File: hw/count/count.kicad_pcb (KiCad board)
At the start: 2 copper layers, 38.4 x 58.9 mm, 22 parts, among them J1 conn_trigger, J2 conn_done, J3 FTDI, J4 Conn_01x01_Male, J5 Conn_01x01_Male, J6 Conn_01x01_Male, J7 Conn_01x01_Male, SW1 reset_count, SW3 switch_reset, U1 ATmega328P-PU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

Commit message: update hardware
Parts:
- removed J4, J5, J6: Conn_01x01_Male, Connector_PinHeader_2.54mm:PinHeader_1x01_P2.54mm_Vertical
- moved C3 11.4 mm to (159.0, 75.9), turned to 180 degrees
- moved SW1 5.17 mm to (135.8, 115.5)
- moved Y1 4.28 mm to (151.4, 80.3)
- moved C2 3.22 mm to (149.1, 75.9), turned to 0 degrees
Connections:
- H1 pad 1: GND -> Net-(H1-Pad1)
- H2 pad 1: GND -> Net-(H2-Pad1)
- H3 pad 1: GND -> Net-(H3-Pad1)
- H4 pad 1: GND -> Net-(H4-Pad1)
- SW1 pad 4: Net-(SW1-Pad3) -> Net-(SW1-Pad4)
- SW3 pad 4: Net-(SW3-Pad3) -> Net-(SW3-Pad4)
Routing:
- net GND: track 186.2 -> 155.7 mm
- net XTAL2: track 30.1 -> 20.3 mm
- net a3: track 26.7 -> 32.2 mm
- net d11: track 5.12 -> 0.00 mm
- net d10: track 4.60 -> 0.00 mm
- net Net-(SW3-Pad3): track 4.50 -> 0.00 mm
- net Net-(SW1-Pad3): track 4.50 -> 0.00 mm
- net d9: track 4.16 -> 0.00 mm
- net VCC: track 127.8 -> 130.1 mm
- net d13: track 37.9 -> 38.5 mm
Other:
- board text added: "v1.1"
- board text removed: "v1"

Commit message: COUNT block v2
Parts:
- removed J2: conn_done, Connector_PinHeader_2.54mm:PinHeader_1x03_P2.54mm_Vertical
- removed J7: Conn_01x01_Male, Connector_PinHeader_2.54mm:PinHeader_1x01_P2.54mm_Vertical
- removed SW1: reset_count, autoblocks:SW_PUSH_6mm_H5mm
- added D2: DIODE, Diode_SMD:D_0603_1608Metric, F.Cu at (133.5, 122.4)
- added J5: BUS, Connector_PinHeader_2.54mm:PinHeader_2x07_P2.54mm_Vertical, F.Cu at (149.1, 95.0)
- added R4: 10k, Resistor_SMD:R_0603_1608Metric, F.Cu at (146.2, 113.4)
- added R5: 1k, Resistor_SMD:R_0603_1608Metric, F.Cu at (137.4, 122.5)
- added R6: 1k, Resistor_SMD:R_0603_1608Metric, F.Cu at (141.3, 122.4)
- added R7: 1k, Resistor_SMD:R_0603_1608Metric, F.Cu at (146.5, 123.5)
- added SW2: resetCount, autoblocks:SW_PUSH_6mm_H5mm, B.Cu at (138.2, 164.6)
- added SW4: NEXT, Package_DIP:DIP-16_W7.62mm_SMDSocket_SmallPads, F.Cu at (136.4, 141.7)
- added SW6: ID, Package_DIP:DIP-16_W7.62mm_SMDSocket_SmallPads, F.Cu at (136.4, 153.2)
- C1: footprint Capacitor_THT:CP_Radial_Tantal_D6.0mm_P2.50mm -> Capacitor_SMD:C_0603_1608Metric
- C2, C3: footprint Capacitor_THT:C_Disc_D3.0mm_W1.6mm_P2.50mm -> Capacitor_SMD:C_0603_1608Metric
- C4, C5: footprint Capacitor_THT:C_Axial_L5.1mm_D3.1mm_P7.50mm_Horizontal -> Capacitor_SMD:C_0603_1608Metric
- H1, H2, H3, H4: footprint MountingHole:MountingHole_2.2mm_M2 -> MountingHole:MountingHole_3.2mm_M3_Pad
- J1: value conn_trigger -> bootloader; footprint Connector_PinHeader_2.54mm:PinHeader_1x03_P2.54mm_Vertical -> autoblocks:edge_connector_3
- J3: footprint Connector_PinHeader_2.54mm:PinHeader_1x06_P2.54mm_Vertical -> autoblocks:edge_connector_3
- R2: footprint Resistor_THT:R_Axial_DIN0207_L6.3mm_D2.5mm_P10.16mm_Horizontal -> Resistor_SMD:R_0603_1608Metric
- SW3: value switch_reset -> reset; footprint autoblocks:SW_PUSH_6mm_H5mm -> Button_Switch_SMD:SW_SPST_TL3305C
- U1: value ATmega328P-PU -> ATmega328-AU; footprint Package_DIP:DIP-28_W7.62mm -> Package_QFP:TQFP-32_7x7mm_P0.8mm
- U2: moved to B.Cu
- Y1: footprint Crystal:Crystal_HC18-U_Vertical -> Crystal:Crystal_SMD_HC49-SD
- moved H2 103.1 mm to (128.0, 166.6)
- moved H1 102.4 mm to (154.7, 166.6)
- moved C3 47.2 mm to (146.5, 121.4), turned to 0 degrees
- moved C2 43.6 mm to (146.3, 119.4)
- moved H4 39.7 mm to (128.0, 96.8)
- moved Y1 37.5 mm to (152.4, 117.8), turned to 270 degrees
- moved H3 37.3 mm to (154.7, 96.8)
- moved U2 31.9 mm to (143.3, 134.1)
- moved C5 30.5 mm to (136.9, 103.1), turned to 0 degrees
- moved C1 26.6 mm to (146.3, 117.5), turned to 180 degrees
- moved C4 25.8 mm to (136.9, 106.9), turned to 180 degrees
- moved R2 24.7 mm to (133.1, 106.8), turned to 180 degrees
- moved U1 24.6 mm to (137.7, 114.7)
- moved SW3 23.9 mm to (130.1, 103.4), turned to 180 degrees
- moved J3 12.9 mm to (126.5, 109.5), turned to 270 degrees
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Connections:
- C1 pad 1: VCC -> bus11
- C1 pad 2: GND -> bus13
- C2 pad 1: GND -> bus13
- C3 pad 1: GND -> bus13
- C4 pad 2: GND -> bus13
- J1 pad 1: a0 -> bus13
- J1 pad 2: GND -> bus11
- J1 pad 3: VCC -> d10
- J3 pad 1: GND -> bus13
- J3 pad 2: GND -> bus13
- J3 pad 3: VCC -> bus11
- R2 pad 1: VCC -> bus11
- SW3 pad 1: GND -> bus13
- U1 pad 1: RESET -> d3
- U1 pad 10: XTAL2 -> d6
- U1 pad 11: d5 -> d7
- U1 pad 12: d6 -> d8
- U1 pad 13: d7 -> d9
- U1 pad 14: d8 -> d10
- U1 pad 15: d9 -> d11
- U1 pad 16: d10 -> d12
- U1 pad 17: d11 -> d13
- U1 pad 18: d12 -> bus11
- U1 pad 19: d13 -> Net-(U1-Pad19)
- U1 pad 2: RX -> d4
- U1 pad 20: VCC -> AREF
- U1 pad 21: AREF -> bus13
- U1 pad 22: GND -> Net-(U1-Pad22)
- U1 pad 3: TX -> bus13
- U1 pad 4: d2 -> bus11
- U1 pad 5: d3 -> bus13
- U1 pad 6: d4 -> bus11
- U1 pad 7: VCC -> XTAL1
- U1 pad 8: GND -> XTAL2
- U1 pad 9: XTAL1 -> d5
- U2 pad 1: d13 -> Net-(R5-Pad2)
- U2 pad 5: a4 -> Net-(R6-Pad2)
- U2 pad 7: a5 -> Net-(R7-Pad2)
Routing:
- net GND: track 155.7 -> 0.00 mm
- net d10: track 0.00 -> 132.1 mm, vias 0 -> 2
- net VCC: track 130.1 -> 0.00 mm
- net bus11: track 0.00 -> 126.7 mm, vias 0 -> 7
- net d11: track 0.00 -> 101.0 mm, vias 0 -> 1
- net d12: track 22.1 -> 107.6 mm, vias 0 -> 2
- net bus2: track 0.00 -> 69.1 mm, vias 0 -> 1
- net bus3: track 0.00 -> 63.8 mm, vias 0 -> 1
- net bus13: track 0.00 -> 63.6 mm, vias 0 -> 6
- net bus5: track 0.00 -> 62.7 mm, vias 0 -> 1
- net bus4: track 0.00 -> 61.4 mm, vias 0 -> 1
- net bus7: track 0.00 -> 61.2 mm, vias 0 -> 1
- net bus1: track 0.00 -> 60.8 mm, vias 0 -> 1
- net bus6: track 0.00 -> 60.3 mm, vias 0 -> 1
- net bus8: track 0.00 -> 59.2 mm, vias 0 -> 1
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- added copper zone on B.Cu, net bus11
- added copper zone on F.Cu, net bus13
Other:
- board size 38.4 x 58.9 mm -> 34.3 x 77.5 mm
- rule trace_min: 0.2 -> 0.16
- board text added: "BOOT"
- board text added: "FTDI"
- board text added: "First"
- board text added: "ID"
- board text added: "NEXT"
- board text added: "Next"
- board text added: "RESET COUNT"
- board text added: "v2"
- board text removed: "COUNTER"
- board text removed: "IN"
- board text removed: "OUT"
- board text removed: "RESET"
- board text removed: "RTS"
- board text removed: "v1.1"

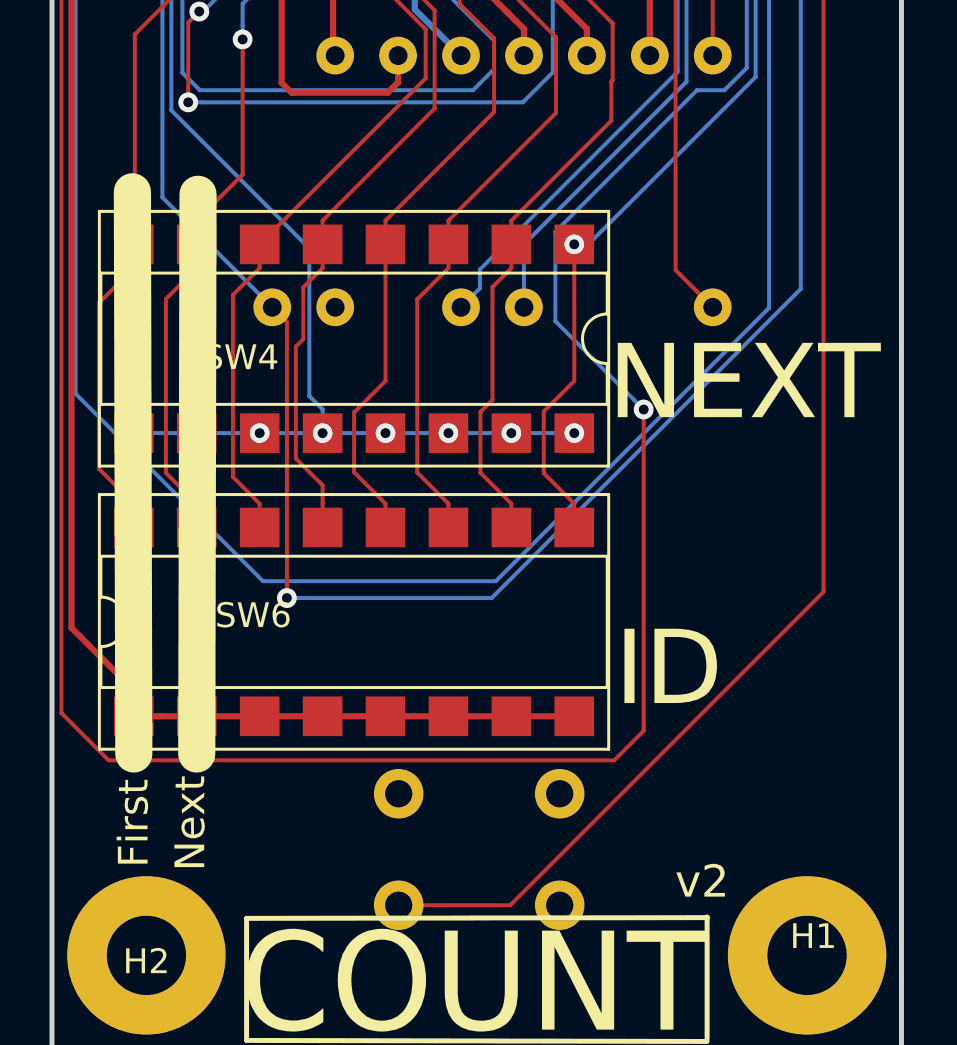
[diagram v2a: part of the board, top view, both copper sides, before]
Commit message: fix COUNT bus assigments
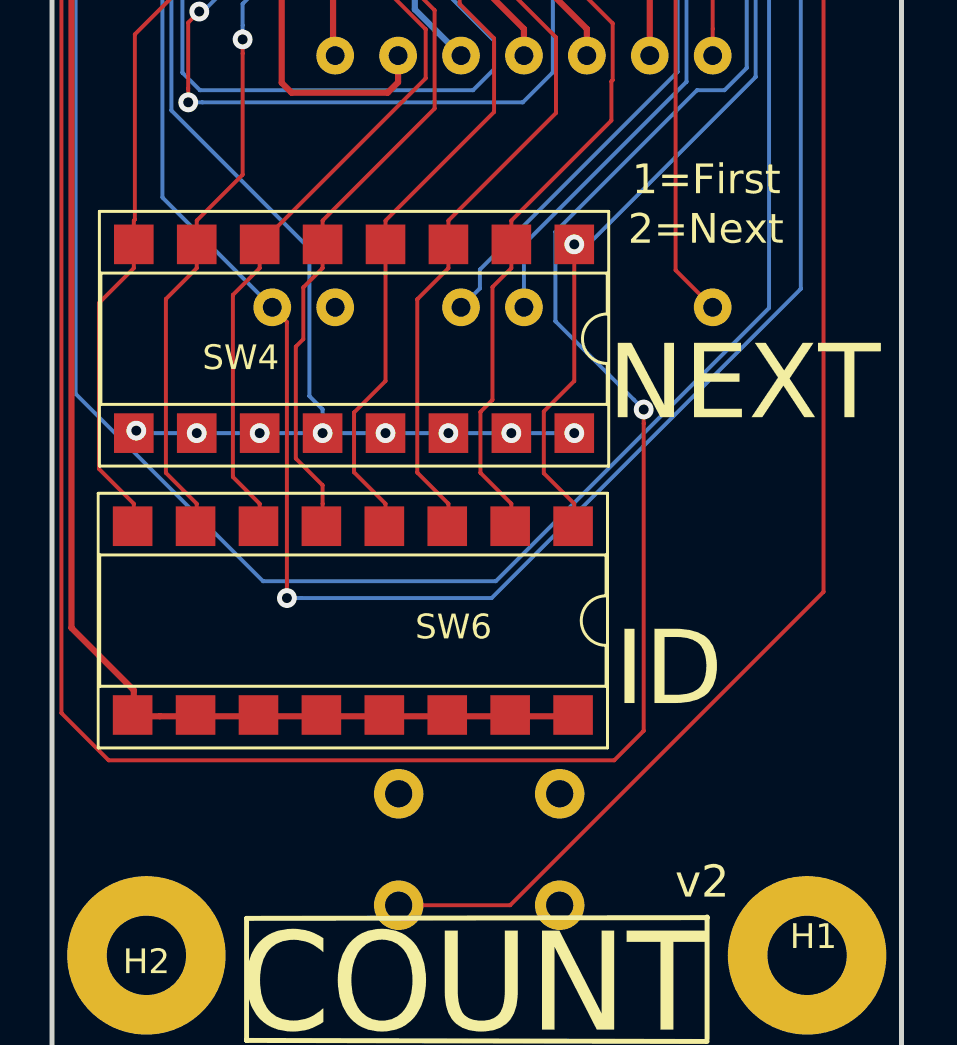
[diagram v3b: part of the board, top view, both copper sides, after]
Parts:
- moved SW6 0.07 mm to (136.3, 153.1), turned to 270 degrees
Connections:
- SW6 pad 1: a0 -> bus1
- SW6 pad 10: bus2 -> a0
- SW6 pad 11: bus3 -> a0
- SW6 pad 12: bus4 -> a0
- SW6 pad 13: bus5 -> a0
- SW6 pad 14: bus6 -> a0
- SW6 pad 15: bus7 -> a0
- SW6 pad 16: bus8 -> a0
- SW6 pad 2: a0 -> bus2
- SW6 pad 3: a0 -> bus3
- SW6 pad 4: a0 -> bus4
- SW6 pad 5: a0 -> bus5
- SW6 pad 6: a0 -> bus6
- SW6 pad 7: a0 -> bus7
- SW6 pad 8: a0 -> bus8
- SW6 pad 9: bus1 -> a0
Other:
- board text added: "1=First"
- board text added: "2=Next"
- board text removed: "First"
- board text removed: "Next"
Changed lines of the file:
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@@
   (general
     (thickness 1.6)
-    (drawings 27)
+    (drawings 25)
     (tracks 679)
     (zones 0)
@@
   )
   (setup
-    (last_trace_width 0.16)
+    (last_trace_width 0.25)
     (user_trace_width 0.16)
     (user_trace_width 1)
@@
   )
   (module Package_DIP:DIP-16_W7.62mm_SMDSocket_SmallPads (layer F.Cu)
-    (at 136.398 153.162 90)
+    (at 136.35 153.11 270)
     (descr "16-lead though-hole mounted DIP package, row spacing 7.62 mm (300 mils), SMDSocket, SmallPads")
     (tags "THT DIP DIL PDIP 2.54mm 7.62mm 300mil SMDSocket SmallPads")
     (attr smd)
-    (fp_text reference SW6 (at 0.254 -4.064 180) (layer F.SilkS)
-      (effects (font (size 1 1) (thickness 0.15)))
-    )
-    (fp_text value ID (at 0 11.22 90) (layer F.Fab)
+    (fp_text reference SW6 (at 0.254 -4.064) (layer F.SilkS)
+      (effects (font (size 1 1) (thickness 0.15)))
+    )
+    (fp_text value ID (at 0 11.22 270) (layer F.Fab)
       (effects (font (size 1 1) (thickness 0.15)))
     )
@@
     (fp_line (start 5.35 10.5) (end 5.35 -10.5) (layer F.CrtYd) (width 0.05))
     (fp_line (start 5.35 -10.5) (end -5.35 -10.5) (layer F.CrtYd) (width 0.05))
-    (fp_text user %R (at 0 0 90) (layer F.Fab)
-      (effects (font (size 1 1) (thickness 0.15)))
-    )
-    (pad 1 smd rect (at -3.81 -8.89 90) (size 1.6 1.6) (layers F.Cu F.Paste F.Mask)
+    (fp_text user %R (at 0 0 270) (layer F.Fab)
+      (effects (font (size 1 1) (thickness 0.15)))
+    )
+    (pad 1 smd rect (at -3.81 -8.89 270) (size 1.6 1.6) (layers F.Cu F.Paste F.Mask)
+      (net 33 bus1))
+    (pad 9 smd rect (at 3.81 8.89 270) (size 1.6 1.6) (layers F.Cu F.Paste F.Mask)
       (net 6 a0))
-    (pad 9 smd rect (at 3.81 8.89 90) (size 1.6 1.6) (layers F.Cu F.Paste F.Mask)
-      (net 33 bus1))
-    (pad 2 smd rect (at -3.81 -6.35 90) (size 1.6 1.6) (layers F.Cu F.Paste F.Mask)
+    (pad 2 smd rect (at -3.81 -6.35 270) (size 1.6 1.6) (layers F.Cu F.Paste F.Mask)
+      (net 34 bus2))
+    (pad 10 smd rect (at 3.81 6.35 270) (size 1.6 1.6) (layers F.Cu F.Paste F.Mask)
       (net 6 a0))
-    (pad 10 smd rect (at 3.81 6.35 90) (size 1.6 1.6) (layers F.Cu F.Paste F.Mask)
-      (net 34 bus2))
-    (pad 3 smd rect (at -3.81 -3.81 90) (size 1.6 1.6) (layers F.Cu F.Paste F.Mask)
+    (pad 3 smd rect (at -3.81 -3.81 270) (size 1.6 1.6) (layers F.Cu F.Paste F.Mask)
+      (net 35 bus3))
+    (pad 11 smd rect (at 3.81 3.81 270) (size 1.6 1.6) (layers F.Cu F.Paste F.Mask)
       (net 6 a0))
-    (pad 11 smd rect (at 3.81 3.81 90) (size 1.6 1.6) (layers F.Cu F.Paste F.Mask)
-      (net 35 bus3))
-    (pad 4 smd rect (at -3.81 -1.27 90) (size 1.6 1.6) (layers F.Cu F.Paste F.Mask)
+    (pad 4 smd rect (at -3.81 -1.27 270) (size 1.6 1.6) (layers F.Cu F.Paste F.Mask)
+      (net 36 bus4))
+    (pad 12 smd rect (at 3.81 1.27 270) (size 1.6 1.6) (layers F.Cu F.Paste F.Mask)
       (net 6 a0))
-    (pad 12 smd rect (at 3.81 1.27 90) (size 1.6 1.6) (layers F.Cu F.Paste F.Mask)
-      (net 36 bus4))
-    (pad 5 smd rect (at -3.81 1.27 90) (size 1.6 1.6) (layers F.Cu F.Paste F.Mask)
+    (pad 5 smd rect (at -3.81 1.27 270) (size 1.6 1.6) (layers F.Cu F.Paste F.Mask)
+      (net 37 bus5))
+    (pad 13 smd rect (at 3.81 -1.27 270) (size 1.6 1.6) (layers F.Cu F.Paste F.Mask)
       (net 6 a0))
-    (pad 13 smd rect (at 3.81 -1.27 90) (size 1.6 1.6) (layers F.Cu F.Paste F.Mask)
-      (net 37 bus5))
-    (pad 6 smd rect (at -3.81 3.81 90) (size 1.6 1.6) (layers F.Cu F.Paste F.Mask)
+    (pad 6 smd rect (at -3.81 3.81 270) (size 1.6 1.6) (layers F.Cu F.Paste F.Mask)
+      (net 38 bus6))
+    (pad 14 smd rect (at 3.81 -3.81 270) (size 1.6 1.6) (layers F.Cu F.Paste F.Mask)
       (net 6 a0))
-    (pad 14 smd rect (at 3.81 -3.81 90) (size 1.6 1.6) (layers F.Cu F.Paste F.Mask)
-      (net 38 bus6))
-    (pad 7 smd rect (at -3.81 6.35 90) (size 1.6 1.6) (layers F.Cu F.Paste F.Mask)
+    (pad 7 smd rect (at -3.81 6.35 270) (size 1.6 1.6) (layers F.Cu F.Paste F.Mask)
+      (net 39 bus7))
+    (pad 15 smd rect (at 3.81 -6.35 270) (size 1.6 1.6) (layers F.Cu F.Paste F.Mask)
       (net 6 a0))
-    (pad 15 smd rect (at 3.81 -6.35 90) (size 1.6 1.6) (layers F.Cu F.Paste F.Mask)
-      (net 39 bus7))
-    (pad 8 smd rect (at -3.81 8.89 90) (size 1.6 1.6) (layers F.Cu F.Paste F.Mask)
+    (pad 8 smd rect (at -3.81 8.89 270) (size 1.6 1.6) (layers F.Cu F.Paste F.Mask)
+      (net 40 bus8))
+    (pad 16 smd rect (at 3.81 -8.89 270) (size 1.6 1.6) (layers F.Cu F.Paste F.Mask)
       (net 6 a0))
-    (pad 16 smd rect (at 3.81 -8.89 90) (size 1.6 1.6) (layers F.Cu F.Paste F.Mask)
-      (net 40 bus8))
     (model ${KISYS3DMOD}/Package_DIP.3dshapes/DIP-16_W7.62mm_SMDSocket.wrl
       (at (xyz 0 0 0))
@@
     (effects (font (size 1.3 1.3) (thickness 0.15)))
   )
-  (gr_line (start 130.1 135.9) (end 130.048 158.496) (layer F.SilkS) (width 1.5))
-  (gr_line (start 127.45 135.8) (end 127.508 158.496) (layer F.SilkS) (width 1.5))
-  (gr_text Next (at 129.794 161.29 90) (layer F.SilkS)
+  (gr_text 2=Next (at 150.6 137.3) (layer F.SilkS)
     (effects (font (size 1.2 1.2) (thickness 0.2)))
   )
-  (gr_text First (at 127.508 161.29 90) (layer F.SilkS)
+  (gr_text 1=First (at 150.62 135.3) (layer F.SilkS)
     (effects (font (size 1.2 1.2) (thickness 0.2)))
   )
